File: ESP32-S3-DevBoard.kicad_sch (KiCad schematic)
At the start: 4 parts, among them J1 USB_C_Receptacle_USB2.0_14P, U1 ESP32-S3-WROOM-1

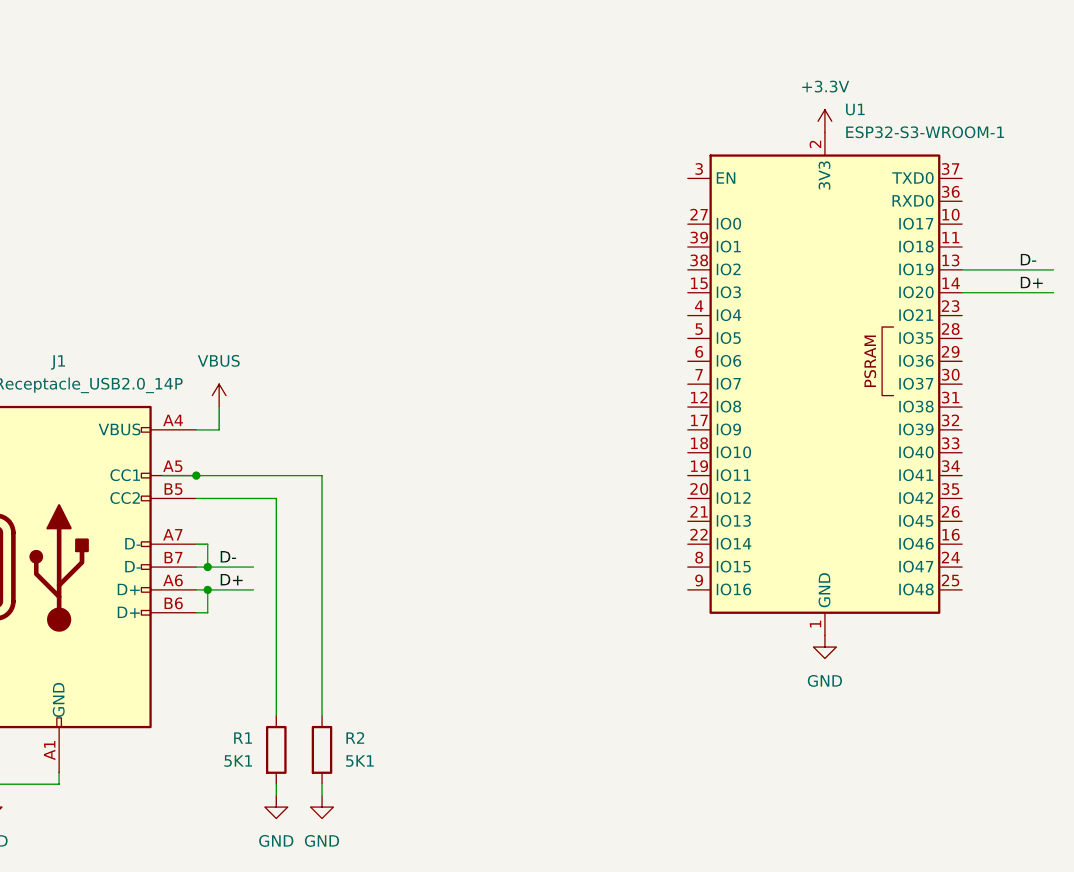
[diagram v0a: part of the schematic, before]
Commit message: Change to global tags
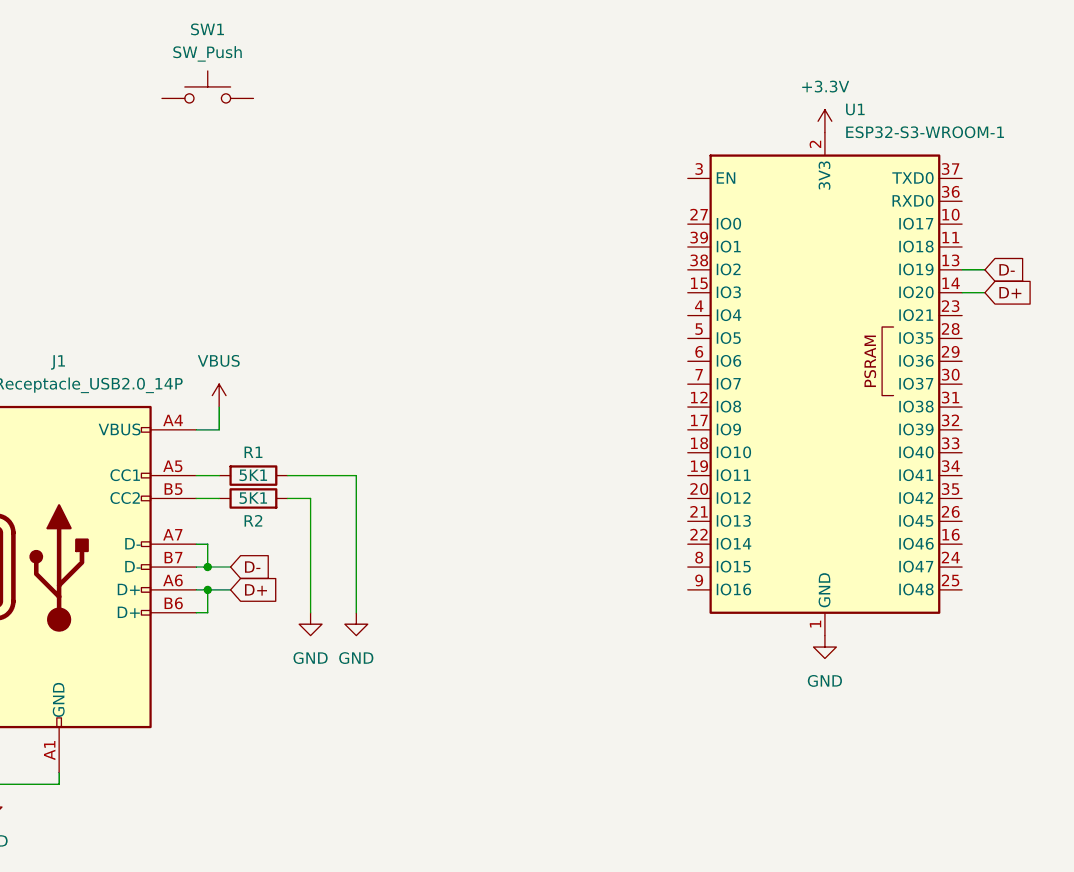
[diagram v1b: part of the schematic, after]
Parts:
- added SW1: SW_Push, symbol Switch:SW_Push
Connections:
- net GND: now also R1.1; no longer R1.2
- net at J1.A5 (CC1): now also R1.2; no longer R2.1
- net at J1.B5 (CC2): now also R2.1; no longer R1.1

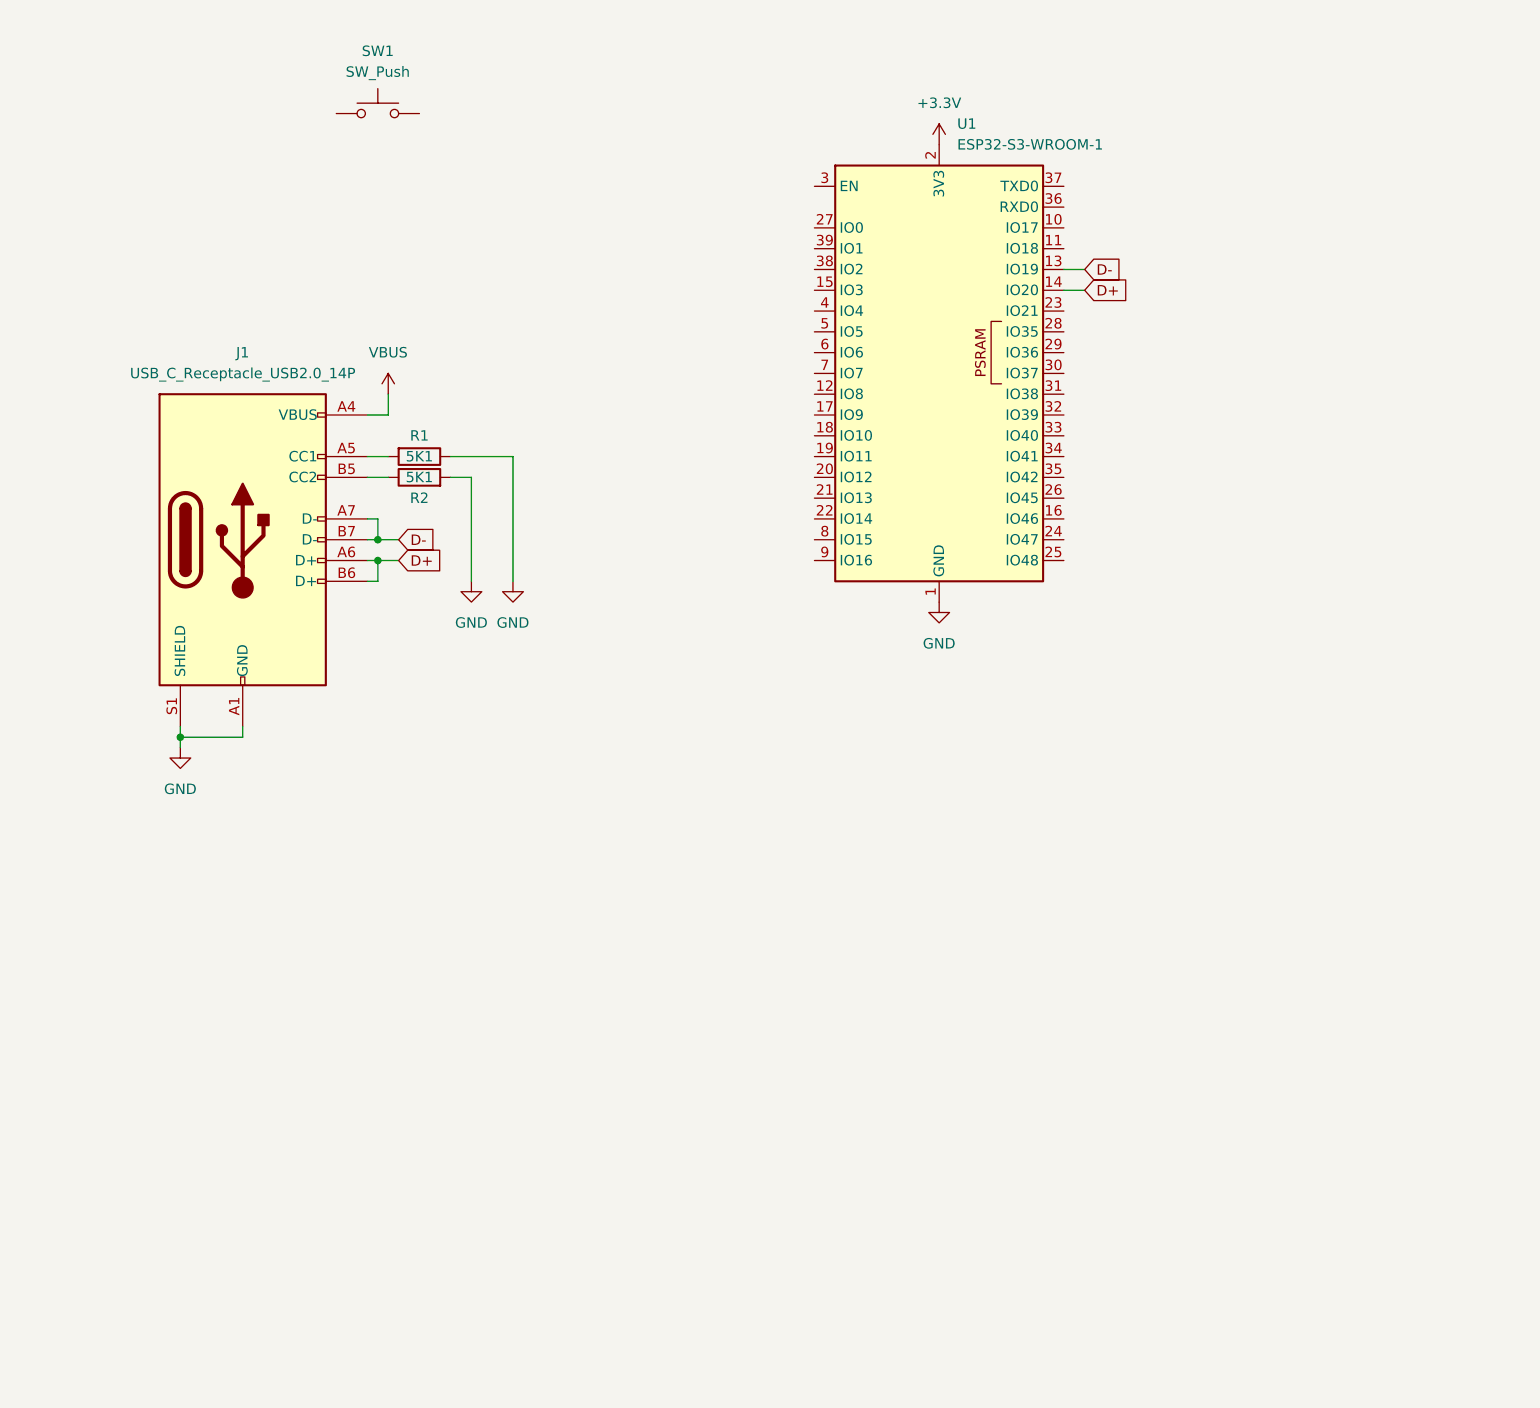
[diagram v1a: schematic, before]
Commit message: Add USB protection
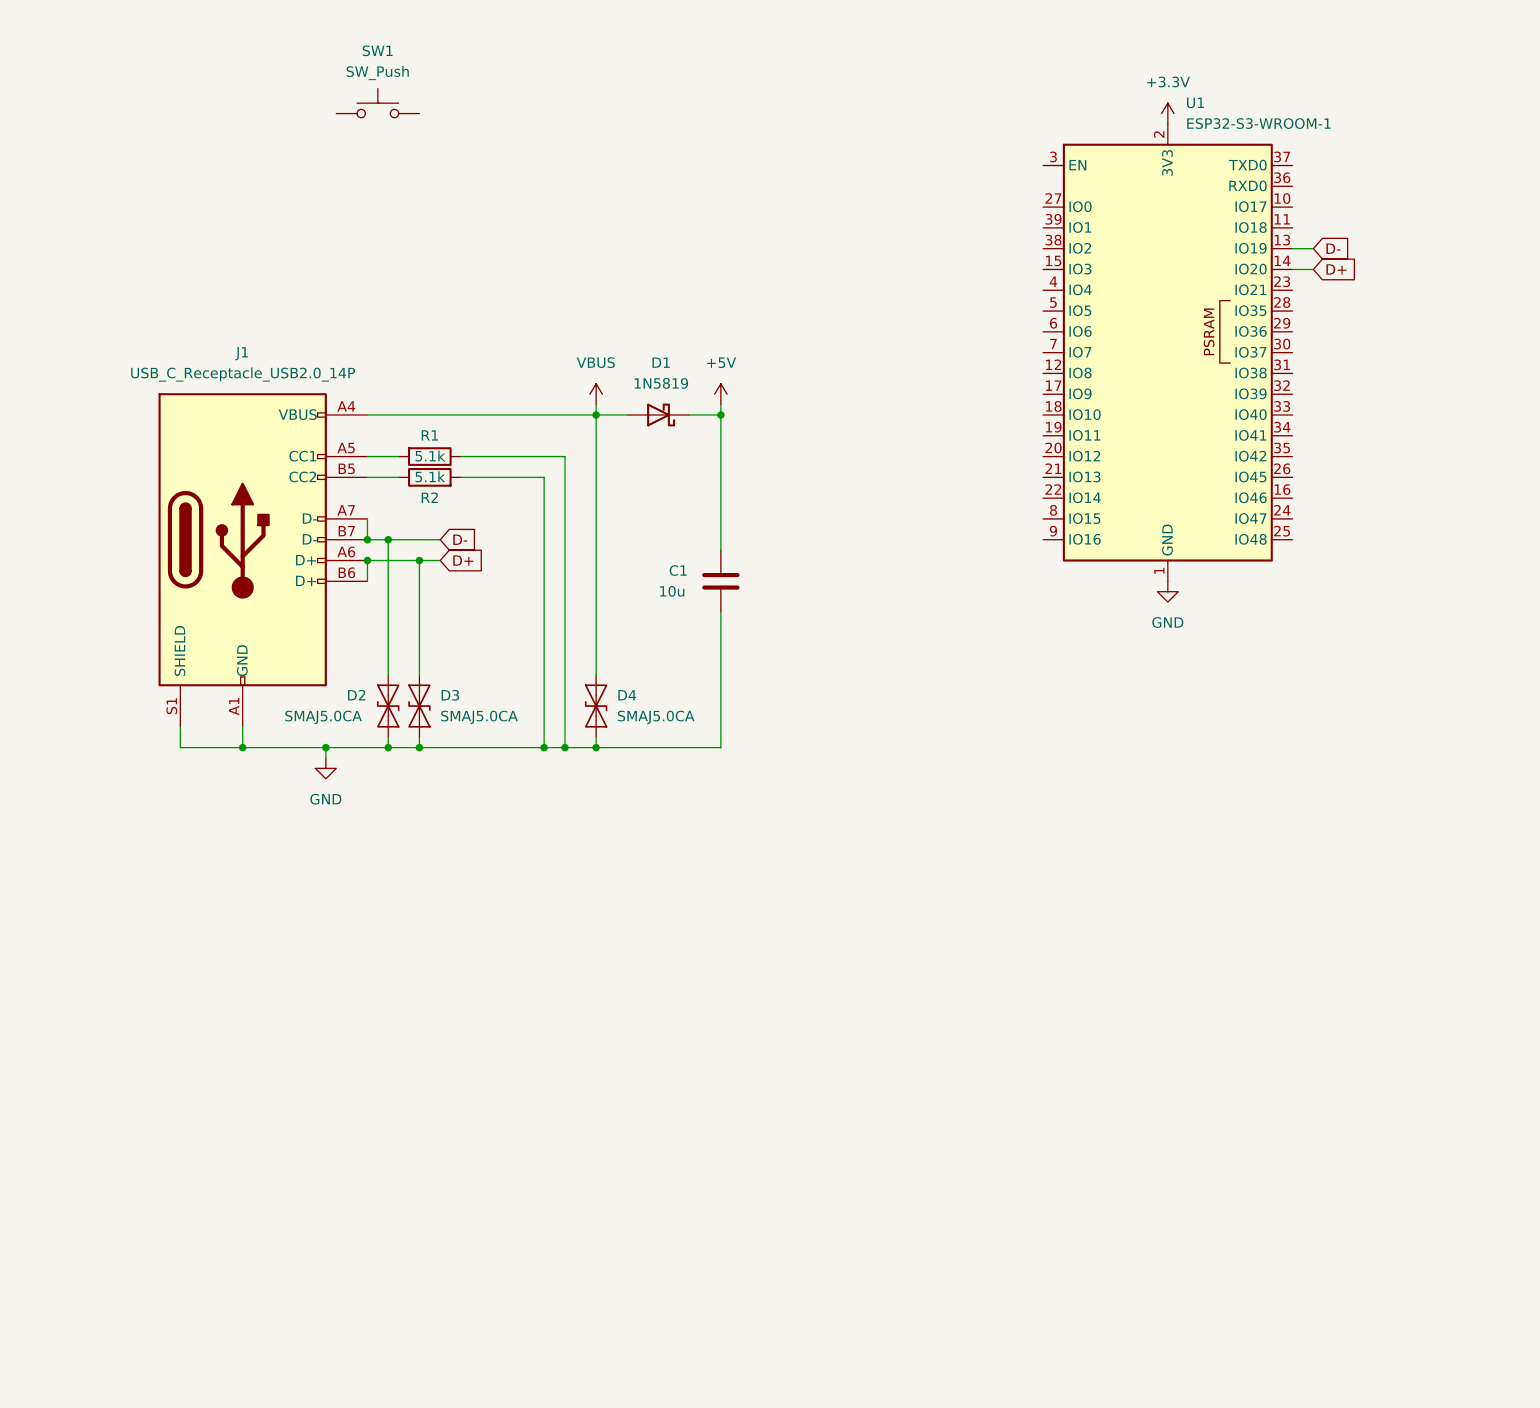
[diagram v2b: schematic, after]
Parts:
- added C1: 10u, symbol Device:C
- added D1: 1N5819, Diode_THT:D_DO-41_SOD81_P10.16mm_Horizontal, symbol Diode:1N5819
- added D2, D3, D4: SMAJ5.0CA, Diode_SMD:D_SMA, symbol Diode:SMAJ5.0CA
- R1, R2: value 5K1 -> 5.1k
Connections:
- net D+: now also D3.2 (A2)
- net D-: now also D2.2 (A2)
- net GND: now also C1.2, D2.1 (A1), D3.1 (A1), D4.1 (A1)
- net VBUS: now also D1.2 (A), D4.2 (A2)
- new net +5V: C1.1, D1.1 (K)
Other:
- moved on the sheet: R1, R2, U1

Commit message: Add voltage regulator
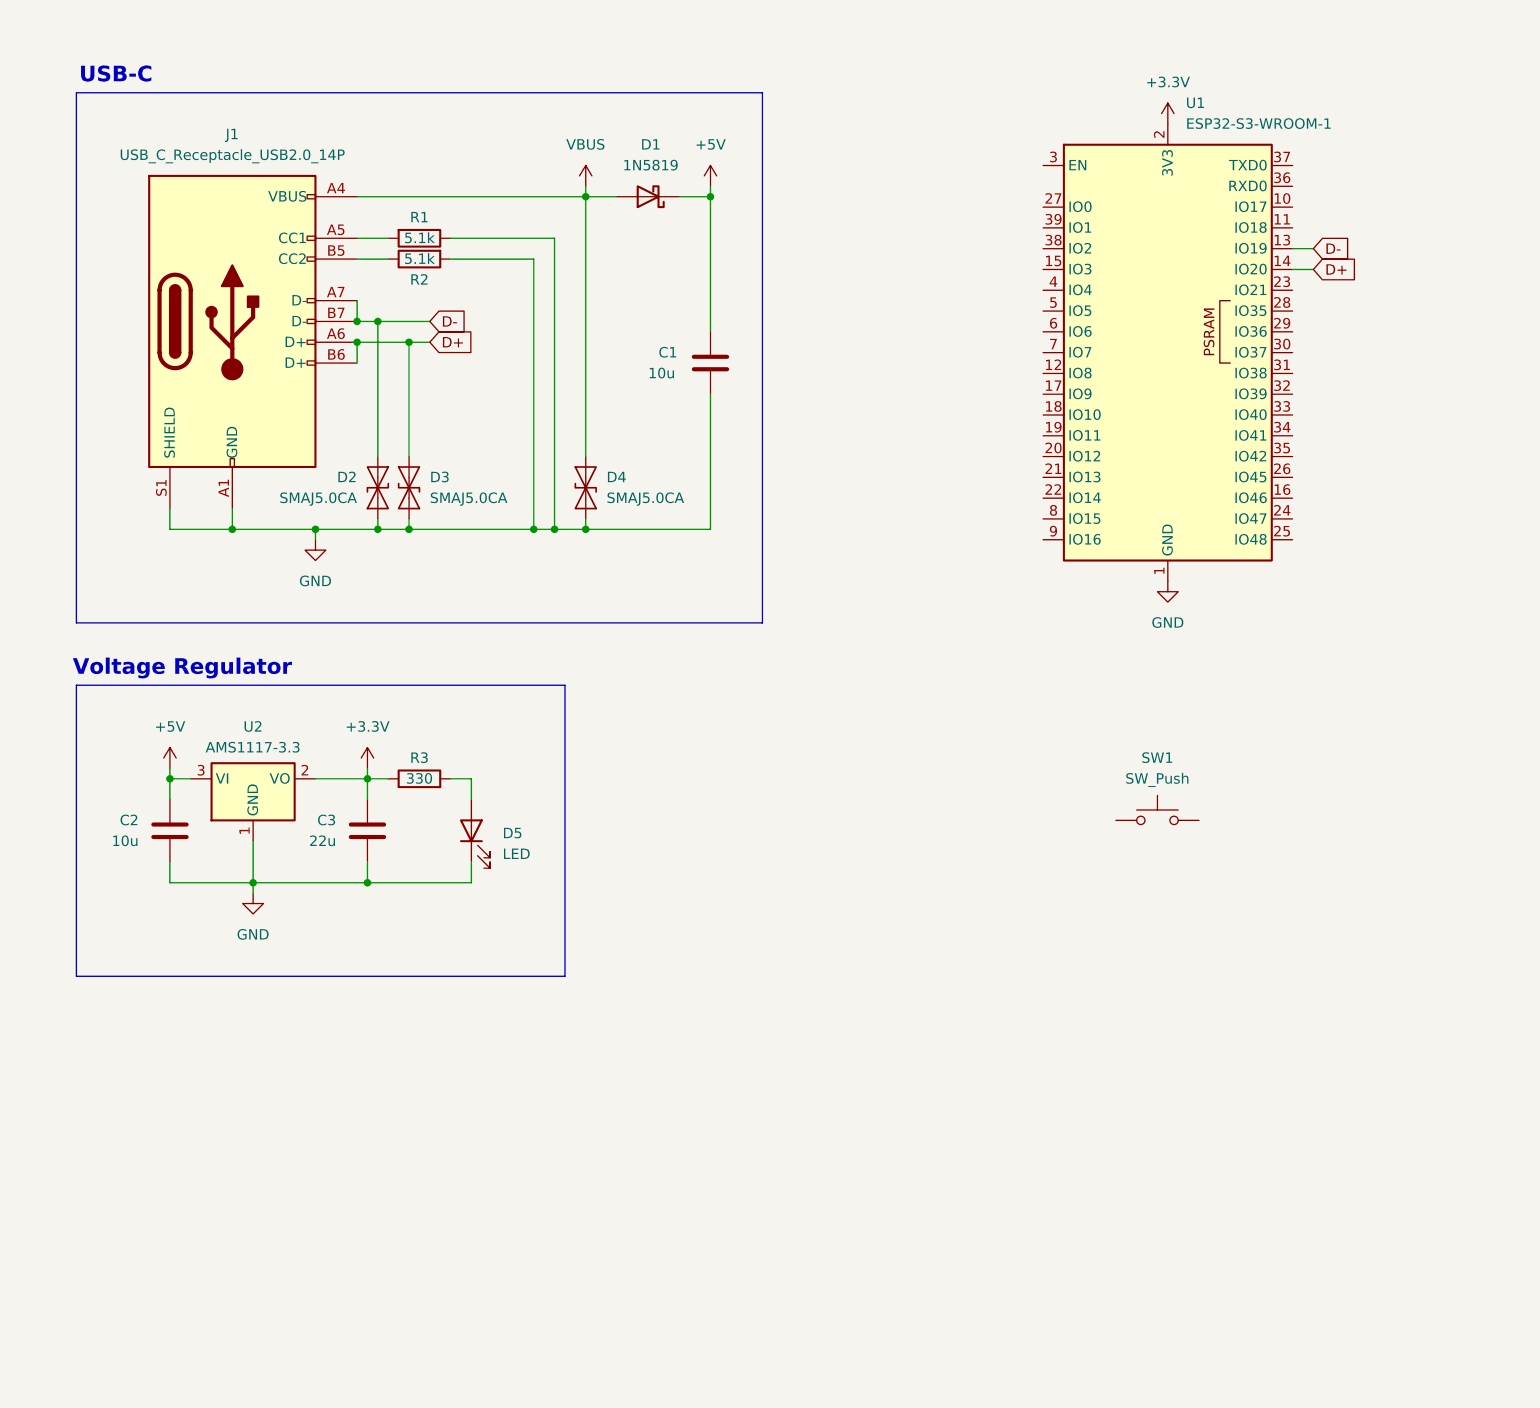
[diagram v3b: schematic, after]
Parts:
- added C2: 10u, symbol Device:C
- added C3: 22u, symbol Device:C
- added D5: LED, symbol Device:LED
- added R3: 330, symbol Device:R
- added U2: AMS1117-3.3, Package_TO_SOT_SMD:SOT-223-3_TabPin2, symbol Regulator_Linear:AMS1117-3.3
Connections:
- net +3.3V: now also C3.1, R3.1, U2.2 (VO)
- net +5V: now also C2.1, U2.3 (VI)
- net GND: now also C2.2, C3.2, D5.1 (K), U2.1 (GND)
- new net: D5.2 (A), R3.2
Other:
- note added: "USB-C"
- note added: "Voltage Regulator"
- moved on the sheet: C1, D1, D2, D3, D4, J1, R1, R2, SW1
